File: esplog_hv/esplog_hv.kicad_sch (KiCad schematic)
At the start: 34 parts, among them IC1 MP2359DJ-LF-Z, SW1 SW_Push, U1 ESP32-C3, U2 BMI160, Y1 Crystal_GND24

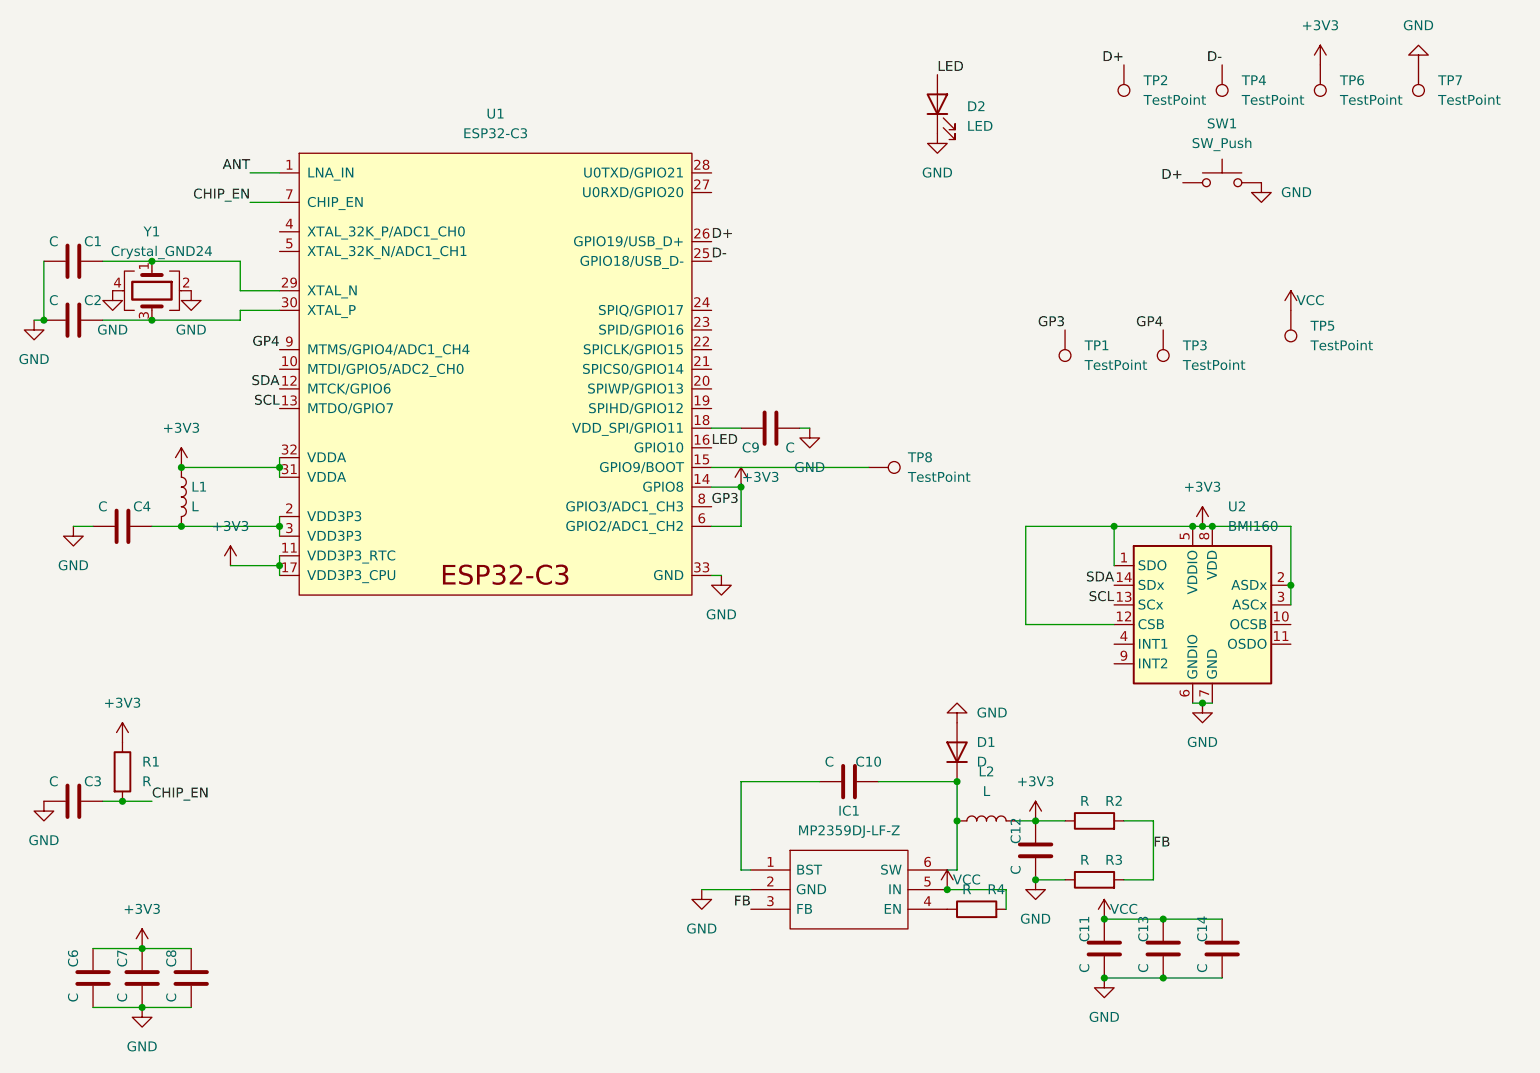
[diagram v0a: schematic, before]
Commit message: Add component values
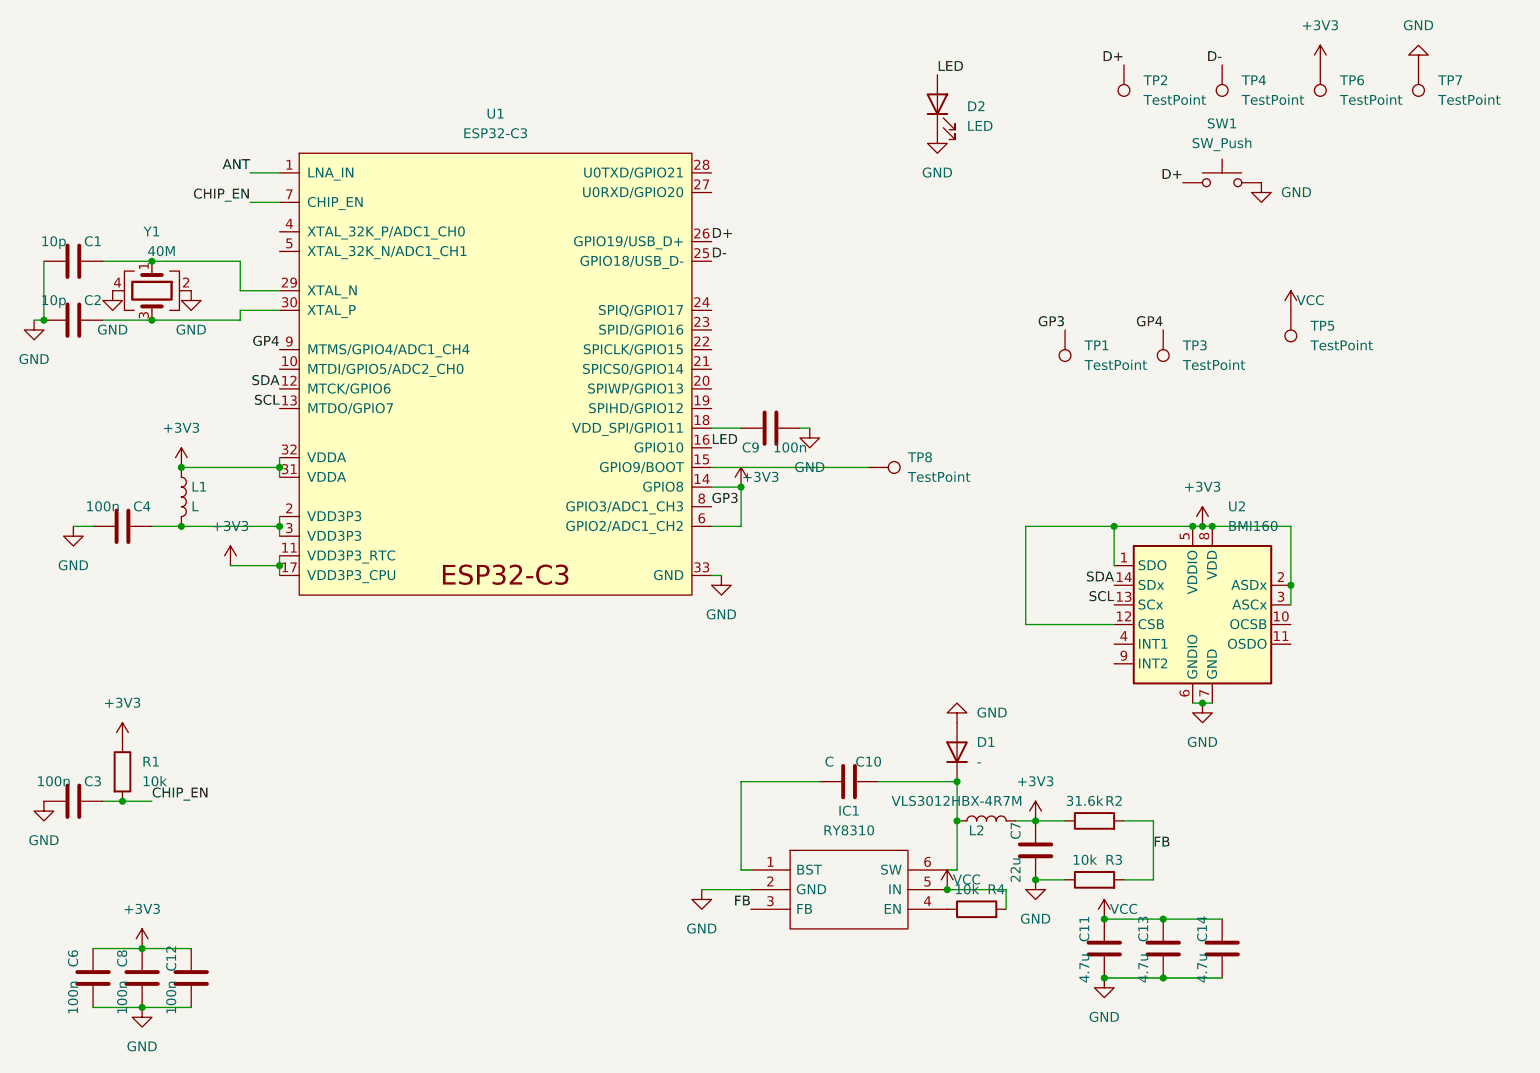
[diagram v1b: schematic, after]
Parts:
- C1, C2: value C -> 10p
- C11, C13, C14: value C -> 4.7u
- C12, C3, C4, C6, C8, C9: value C -> 100n
- C7: value C -> 22u
- D1: value D -> -; now left out of the parts list
- IC1: value MP2359DJ-LF-Z -> RY8310
- L2: value L -> VLS3012HBX-4R7M
- R1, R3, R4: value R -> 10k
- R2: value R -> 31.6k
- Y1: value Crystal_GND24 -> 40M
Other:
- moved on the sheet: C12, C7, C8

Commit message: esplog_hv: change the capacitor value on chip_en to 1u
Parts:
- C3: value 100n -> 1u
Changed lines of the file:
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@@
     (in_bom yes) (on_board yes)
     (property "Reference" "C3" (id 0) (at 93.98 134.62 90))
-    (property "Value" "100n" (id 1) (at 88.9 134.62 90))
+    (property "Value" "1u" (id 1) (at 88.9 134.62 90))
     (property "Footprint" "Capacitor_SMD:C_0402_1005Metric" (id 2) (at 95.25 136.1948 0)
       (effects (font (size 1.27 1.27)) hide)
@@
     )
     (path "/b0061c6b-e8c7-4f80-b07f-9febe7a410d4"
-      (reference "C3") (unit 1) (value "100n") (footprint "Capacitor_SMD:C_0402_1005Metric")
+      (reference "C3") (unit 1) (value "1u") (footprint "Capacitor_SMD:C_0402_1005Metric")
     )
     (path "/9814b1e2-94b2-4a42-b7b9-8afdf2af0d80"

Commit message: add gerbers for esplog-hv
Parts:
- L1: value L -> 2n
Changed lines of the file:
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@@
       (effects (font (size 1.27 1.27)) (justify left))
     )
-    (property "Value" "L" (id 1) (at 106.68 99.0599 0)
+    (property "Value" "2n" (id 1) (at 106.68 99.0599 0)
       (effects (font (size 1.27 1.27)) (justify left))
     )
@@
     )
     (path "/f9db7adc-2b80-427e-97c0-1d4030176bd0"
-      (reference "L1") (unit 1) (value "L") (footprint "Inductor_SMD:L_0402_1005Metric")
+      (reference "L1") (unit 1) (value "2n") (footprint "Inductor_SMD:L_0402_1005Metric")
     )
     (path "/8aeb65d0-734a-412b-b050-0bba5aff695f"
